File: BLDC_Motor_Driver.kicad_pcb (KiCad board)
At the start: 2 copper layers, 145 x 96 mm, 92 parts, among them IC1 AS5047P-ATSM, IC10 INA214AIDCKT, IC12 INA214AIDCKT, IC13 INA214AIDCKT, IC2 L6498D, IC3 ATSAMD21G18A-MFT, IC5 ISL21090BFB812Z-TK, IC6 L6498D, IC7 L6498D, IC8 TPS7A4901DGNT, J1 FTSH-105-01-L-DV-K, J2 031-5431-10RFX, J3 031-5431-10RFX, J4 112405-12, J5 Conn_01x05_Pin, J6 Conn_01x04_Socket, J7 112405-12, Q1 IPB320N20N3GATMA1, Q2 IPB320N20N3GATMA1, Q3 IPB320N20N3GATMA1, Q4 IPB320N20N3GATMA1, Q5 IPB320N20N3GATMA1, Q6 IPB320N20N3GATMA1

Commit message: Add 5V rail available for LDO input
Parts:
- added C15: 47uF, BLDC-Motor-Driver:CAPAE660X770N, F.Cu at (86.0, 83.0)
- added J8: 031-5431-10RFX, BLDC-Motor-Driver:031543110RFX, F.Cu at (88.5, 98.0)
- added J9: Conn_01x03_Pin, Connector_PinHeader_2.54mm:PinHeader_1x03_P2.54mm_Vertical, F.Cu at (88.6, 75.6)
- C7: value 220uF -> 100uF; footprint BLDC-Motor-Driver:CAPAE1030X1050N -> BLDC-Motor-Driver:CAPAE830X1050N
- H1, H2, H3, H4: footprint MountingHole:MountingHole_3.2mm_M3_DIN965_Pad -> MountingHole:MountingHole_4.3mm_M4_DIN965_Pad_TopBottom
- H5, H6, H7, H8: value MountingHole -> MountingHole_Pad; footprint MountingHole:MountingHole_4.3mm_M4 -> MountingHole:MountingHole_3.2mm_M3_DIN965_Pad
- J5: moved to F.Cu
- R11, R16, R5: value 50mΩ -> 10mΩ
- moved J2 107.4 mm to (185.8, 42.0), turned to -90 degrees
- moved C9 89.9 mm to (177.8, 45.0), turned to 90 degrees
- moved J3 23.6 mm to (89.0, 56.0)
- moved J5 20.8 mm to (155.8, 65.8), turned to -90 degrees
- moved R6 17.9 mm to (84.2, 105.2)
- moved R19 17.9 mm to (88.1, 105.2)
- moved J1 17.8 mm to (85.5, 110.5)
- moved G*** 14.3 mm to (83.6, 125.3)
- moved H7 14.0 mm to (77.4, 138.9)
- moved H5 13.1 mm to (201.1, 56.0)
- moved R34 13.1 mm to (157.5, 63.0)
- moved C10 12.1 mm to (125.6, 100.9)
- moved C11 12.1 mm to (125.6, 101.9)
- moved C13 12.1 mm to (119.8, 96.7)
- moved C17 12.1 mm to (195.7, 60.7)
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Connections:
- C22 pad 1: +12V -> /LDO_INPUT
- IC8 pad 5: +12V -> /LDO_INPUT
- IC8 pad 8: +12V -> /LDO_INPUT
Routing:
- net VBUS: track 225.2 -> 128.2 mm
- net /LDO_INPUT: track 0.00 -> 37.9 mm
- net /Microcontroller/BENCHMARK_IO_3: track 4.12 -> 39.4 mm, vias 0 -> 2
- net /Microcontroller/BENCHMARK_IO_2: track 6.25 -> 39.4 mm, vias 0 -> 2
- net /Microcontroller/BENCHMARK_IO_1: track 9.67 -> 40.9 mm, vias 0 -> 2
- net +5V: track 0.00 -> 20.0 mm
- net GND: track 66.3 -> 80.6 mm, vias 342 -> 416
- net +12V: track 199.1 -> 190.9 mm
- net /Microcontroller/SWDIO: track 45.3 -> 48.8 mm
- net +3V3: track 301.4 -> 304.6 mm
- net /Microcontroller/RESET: track 38.9 -> 41.9 mm
- net /Microcontroller/SWCLK: track 45.1 -> 47.9 mm
- net /Microcontroller/TCC0_WO5: track 29.8 -> 31.0 mm
- net Net-(D3-A): track 2.96 -> 2.08 mm
- net /Microcontroller/TCC0_WO2: track 48.4 -> 49.0 mm
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- removed copper zone on F.Cu, net (none)
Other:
- board size 145 x 96 mm -> 135 x 111 mm

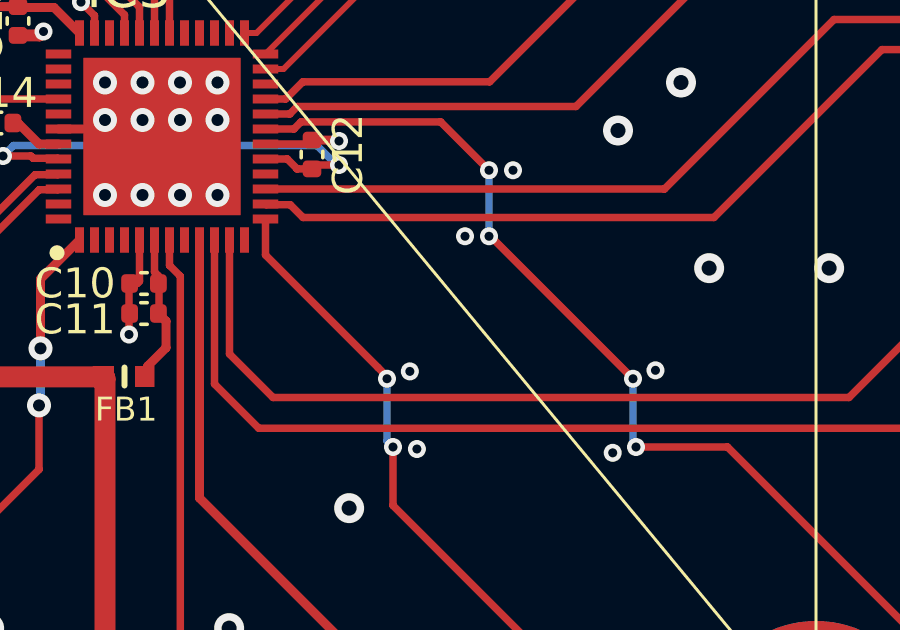
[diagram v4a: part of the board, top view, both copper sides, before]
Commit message: Add more vias
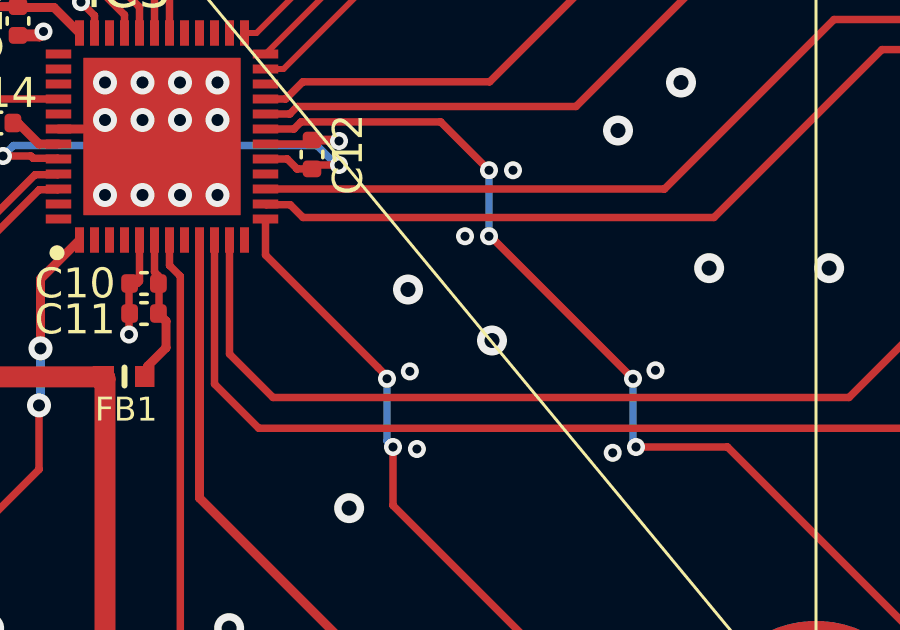
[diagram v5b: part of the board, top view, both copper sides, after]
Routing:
- net GND: vias 416 -> 418
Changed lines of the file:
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@@
+	)
+	(via
+		(at 134.4 101.1)
+		(size 1)
+		(drill 0.5)
+		(layers "F.Cu" "B.Cu")
+		(free yes)
+		(net 7)
 	)
 	(via
@@
 		(layers "F.Cu" "B.Cu")
 		(free yes)
+		(net 7)
+	)
+	(via
+		(at 137.2 102.8)
+		(size 1)
+		(drill 0.5)
+		(layers "F.Cu" "B.Cu")
+		(free yes)
